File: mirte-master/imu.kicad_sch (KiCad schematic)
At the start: 1 part, among them J10 IMU MPU-9250

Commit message: mirte master parts jclpcb fixed
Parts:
- J10: LCSC C37208 -> C2897373
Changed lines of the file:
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@@
       (effects (font (size 1.27 1.27)) hide)
     )
-    (property "LCSC" "C37208" (at 132.08 72.39 0)
+    (property "LCSC" "C2897373" (at 132.08 72.39 0)
       (effects (font (size 1.27 1.27)) hide)
     )

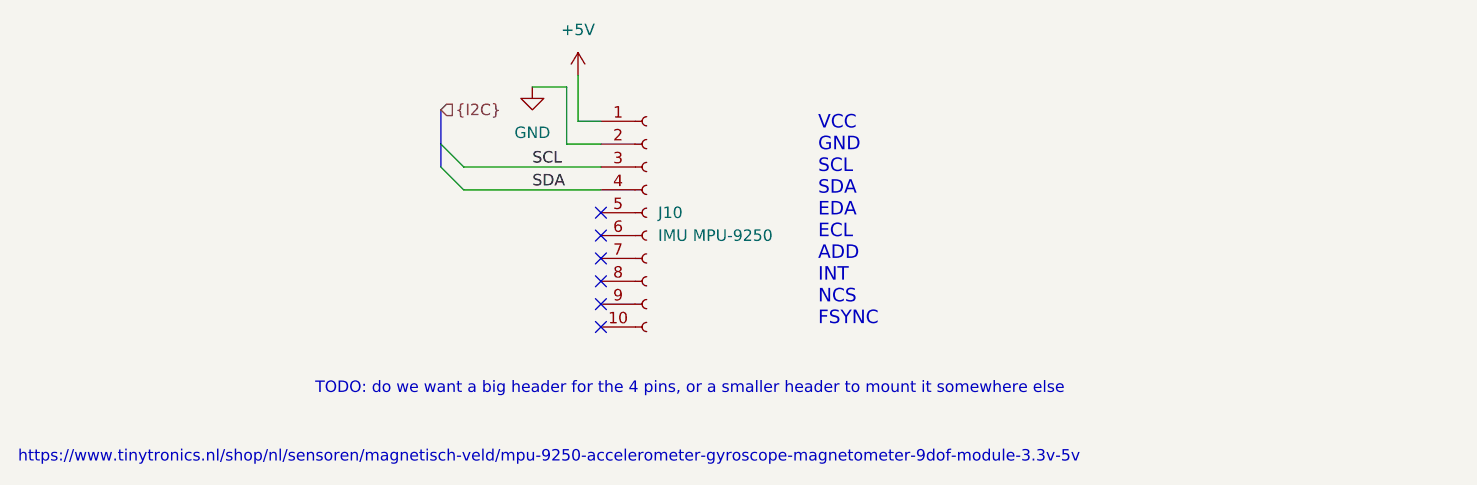
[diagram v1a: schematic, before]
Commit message: mirte-master schematic cleanup and readabilityimprovements
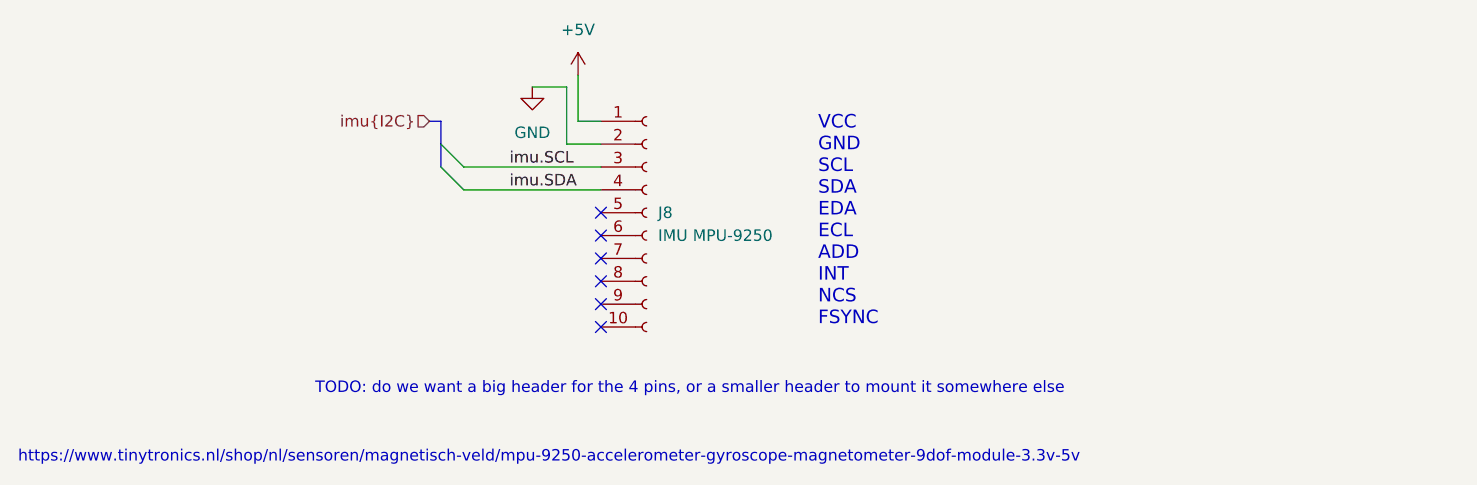
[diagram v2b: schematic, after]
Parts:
- renumbered J10 to J8
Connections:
- net SCL renamed imu.SCL
- net SDA renamed imu.SDA
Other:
- title: (none) -> ${PROJECTNAME}
